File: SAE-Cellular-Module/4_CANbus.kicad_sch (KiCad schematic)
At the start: 20 parts, among them U5 MCP251863T-E-9PX, Y1 4MHz

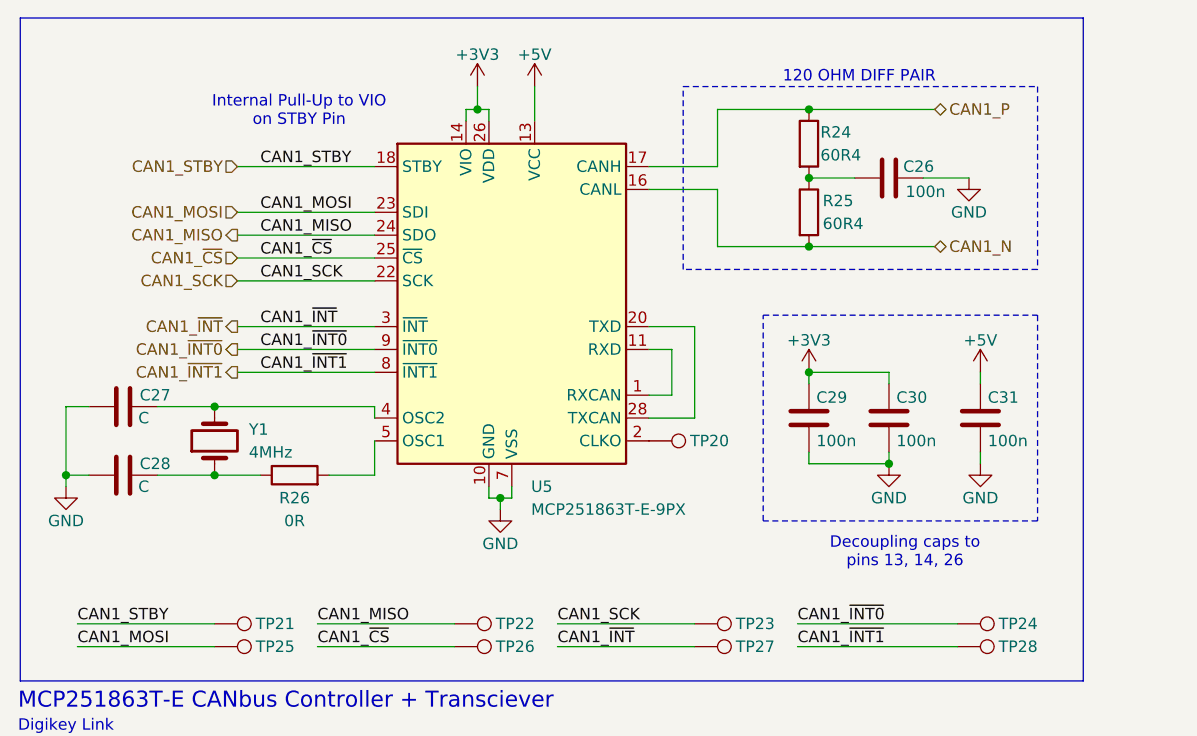
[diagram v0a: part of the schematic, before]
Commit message: Added initial component placements
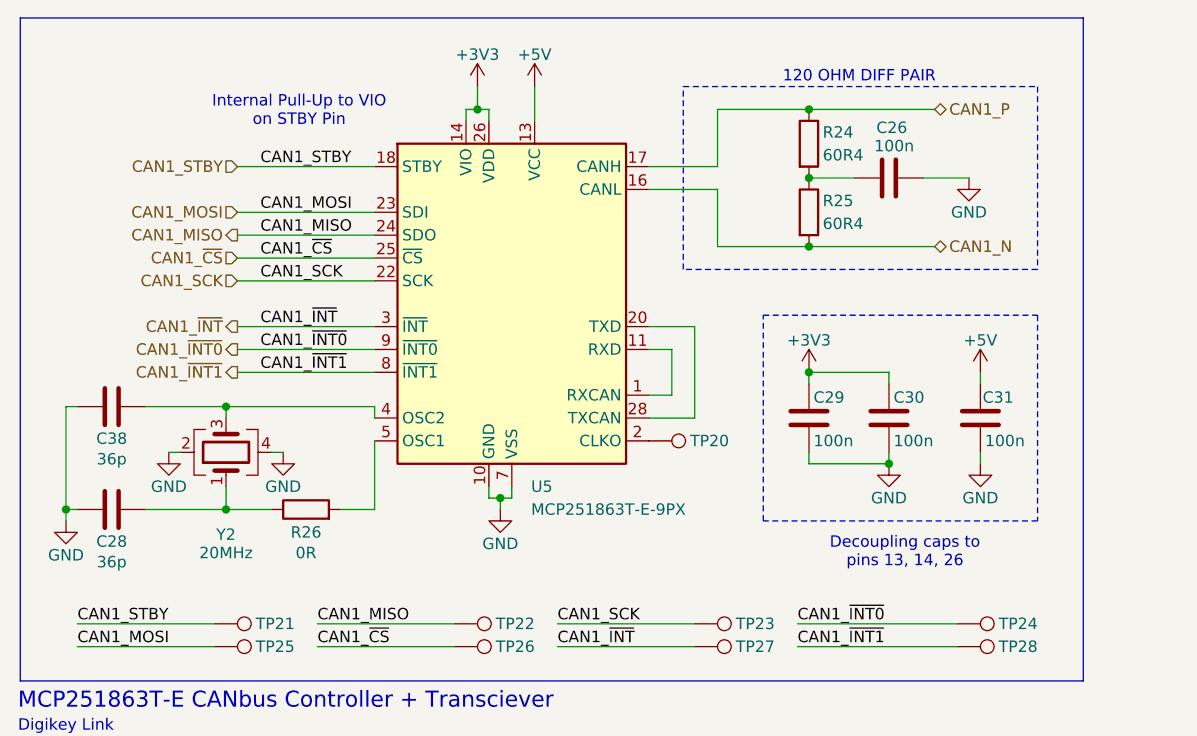
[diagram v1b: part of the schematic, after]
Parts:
- removed C27: C, symbol Device:C
- removed Y1: 4MHz, symbol Device:Crystal
- added C38: 36p, Capacitor_SMD:C_0402_1005Metric, symbol Device:C
- added Y2: 20MHz, Crystal:Crystal_SMD_Abracon_ABM8G-4Pin_3.2x2.5mm, symbol Device:Crystal_GND24
- C26, C29, C30, C31: footprint (none) -> Capacitor_SMD:C_0402_1005Metric; MPN (none) -> CL05B104KP5NNNC
- C28: value C -> 36p; footprint (none) -> Capacitor_SMD:C_0402_1005Metric; MPN (none) -> GCM0335C1H360FA16D
- R24, R25: footprint (none) -> Resistor_SMD:R_0603_1608Metric; MPN (none) -> CR0603-FX-60R4ELF
- R26: footprint (none) -> Resistor_SMD:R_0402_1005Metric; MPN (none) -> RC1005J000CS
- TP20, TP21, TP22, TP23, TP24, TP25, TP26, TP27, TP28: footprint (none) -> TestPoint:TestPoint_Pad_D1.0mm
- U5: footprint Package_DFN_QFN:VQFN-28-1EP_5x5mm_P0.5mm_EP3.25x3.25mm -> MCP251863T_E:VQFN28_9PX_3p25X3p25EPAD_MCH; MPN (none) -> MCP251863T-E-9PX
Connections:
- net +3V3: now also C29.1, C30.1; no longer C29.2, C30.2
- net +5V: now also C31.1; no longer C31.2
- net GND: now also C29.2, C30.2, C31.2, C38.1, Y2.2, Y2.4; no longer C29.1, C30.1, C31.1
- net at C28.2, R26.1: now also Y2.1
- net at U5.4 (OSC2): now also C38.2, Y2.3
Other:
- moved on the sheet: C28, R26
